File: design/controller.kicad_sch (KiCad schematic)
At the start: 23 parts, among them U1 ProMicro

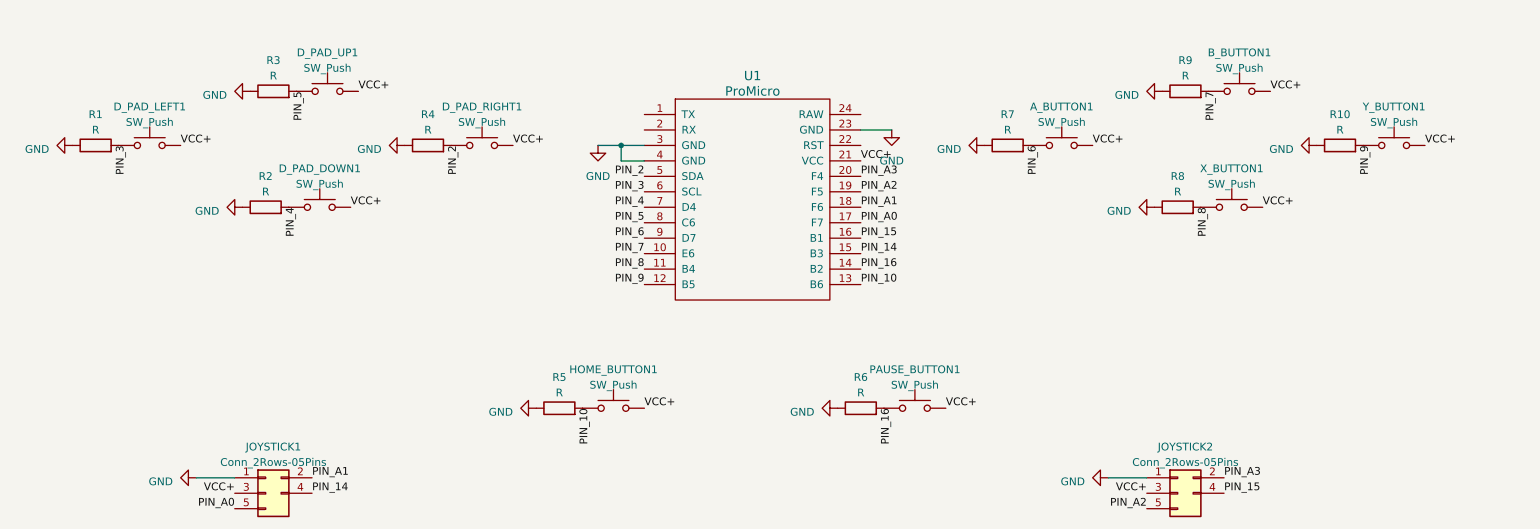
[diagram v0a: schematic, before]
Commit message: Fixing controller design documents
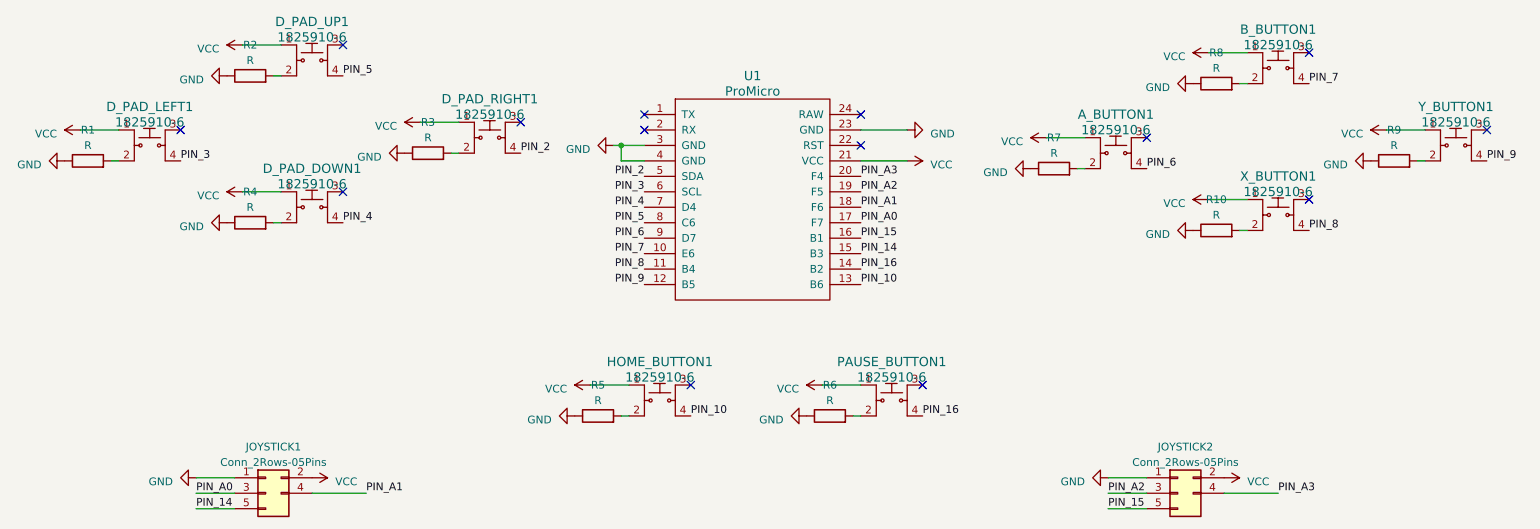
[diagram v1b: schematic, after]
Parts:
- removed A_BUTTON1, B_BUTTON1, D_PAD_DOWN1, D_PAD_LEFT1, D_PAD_RIGHT1, D_PAD_UP1, HOME_BUTTON1, PAUSE_BUTTON1, X_BUTTON1, Y_BUTTON1: SW_Push, Button_Switch_THT:SW_PUSH_6mm_H5mm, symbol Switch:SW_Push
- added A_BUTTON1, B_BUTTON1, D_PAD_DOWN1, D_PAD_LEFT1, D_PAD_RIGHT1, D_PAD_UP1, HOME_BUTTON1, PAUSE_BUTTON1, X_BUTTON1, Y_BUTTON1: 1825910-6, controller:SW_PUSH_4_PIN, symbol dk_Tactile-Switches:1825910-6
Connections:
- net PIN_10: now also HOME_BUTTON1.4
- net PIN_14: now also JOYSTICK1.5 (Pin_5); no longer JOYSTICK1.4 (Pin_4)
- net PIN_15: now also JOYSTICK2.5 (Pin_5); no longer JOYSTICK2.4 (Pin_4)
- net PIN_16: now also PAUSE_BUTTON1.4
- net PIN_2: now also D_PAD_RIGHT1.4
- net PIN_3: now also D_PAD_LEFT1.4
- net PIN_4: now also D_PAD_DOWN1.4
- net PIN_5: now also D_PAD_UP1.4
- net PIN_6: now also A_BUTTON1.4
- net PIN_7: now also B_BUTTON1.4
- net PIN_8: now also X_BUTTON1.4
- net PIN_9: now also Y_BUTTON1.4
- net PIN_A0: now also JOYSTICK1.3 (Pin_3); no longer JOYSTICK1.5 (Pin_5)
- net PIN_A1: now also JOYSTICK1.4 (Pin_4); no longer JOYSTICK1.2 (Pin_2)
- net PIN_A2: now also JOYSTICK2.3 (Pin_3); no longer JOYSTICK2.5 (Pin_5)
- net PIN_A3: now also JOYSTICK2.4 (Pin_4); no longer JOYSTICK2.2 (Pin_2)
- net at R5.2: now also HOME_BUTTON1.2
- net at R8.2: now also B_BUTTON1.2
- net at R6.2: now also PAUSE_BUTTON1.2
- net at R1.2: now also D_PAD_LEFT1.2
- net at R7.2: now also A_BUTTON1.2
- net at R2.2: now also D_PAD_UP1.2
- net at R4.2: now also D_PAD_DOWN1.2
- net at R10.2: now also X_BUTTON1.2
- net at R3.2: now also D_PAD_RIGHT1.2
- net at R9.2: now also Y_BUTTON1.2
- removed net VCC+: JOYSTICK1.3 (Pin_3), JOYSTICK2.3 (Pin_3), U1.21 (VCC)
- new net VCC: A_BUTTON1.1, B_BUTTON1.1, D_PAD_DOWN1.1, D_PAD_LEFT1.1, D_PAD_RIGHT1.1, D_PAD_UP1.1, HOME_BUTTON1.1, JOYSTICK1.2 (Pin_2), JOYSTICK2.2 (Pin_2), PAUSE_BUTTON1.1, U1.21 (VCC), X_BUTTON1.1, Y_BUTTON1.1
- no-connect marks 0 -> 14
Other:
- moved on the sheet: R1
